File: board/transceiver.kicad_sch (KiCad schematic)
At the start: 5 parts, among them U1 TJA1441

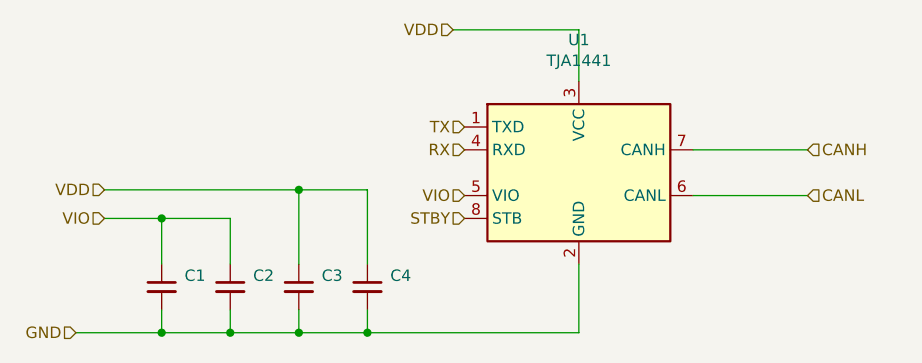
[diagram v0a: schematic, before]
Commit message: changed transceiver chip to be more availible TJA1044GT version
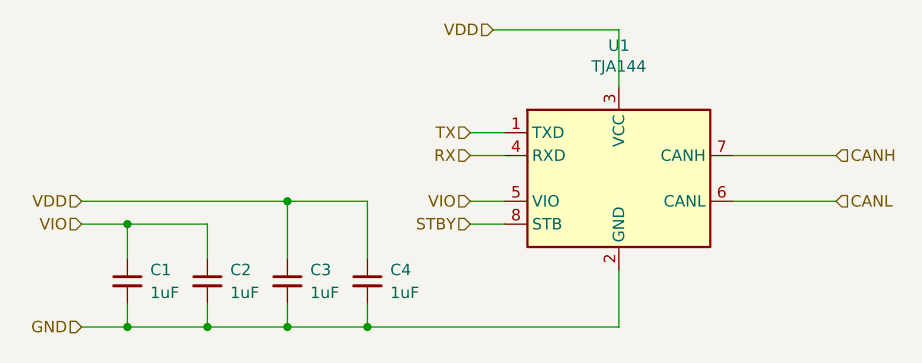
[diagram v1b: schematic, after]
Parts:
- C1, C2, C3, C4: value (none) -> 1uF; footprint (none) -> Capacitor_SMD:C_0603_1608Metric; lcsc (none) -> C15849
- U1: value TJA1441 -> TJA144; lcsc (none) -> C961486
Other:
- moved on the sheet: C1, C2, C3, C4, U1
